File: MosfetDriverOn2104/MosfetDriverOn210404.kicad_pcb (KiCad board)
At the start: 2 copper layers, 83.6 x 89.7 mm, 88 parts, among them J1 I2C HDR, J10 ENCODER HDR, J11 CROSS CONN, J12 motor, J2 AVR-ISP-6, J3 I2C HDR, J4 Screw_Terminal_01x02, J5 I2C HDR, J6 UART HDR, J7 5V HDR, J8 GND HDR, J9 servo hdr, Q1 IRF540N, Q2 IRF540N, Q3 IRF540N, Q4 IRF540N, SW1 SW_Push, SW2 SW_DIP_x04, SW3 SW_Push, SW4 SW_Push, U1 LM2576HVS-ADJ, U2 L7805, U3 IR2104, U4 LM358, U5 IR2104, U6 ATmega328P-AU-MCU_Microchip_A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

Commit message: Tested Route capability
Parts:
- moved CB6 11.5 mm to (141.8, 100.7), turned to 0 degrees
- moved R10 0.51 mm to (149.3, 128.3)
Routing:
- net GND: track 0.00 -> 495.8 mm, vias 0 -> 1
- net VCC: track 0.00 -> 225.2 mm
- net +5V: track 0.00 -> 177.9 mm, vias 0 -> 3
- net +15V: track 0.00 -> 149.8 mm, vias 0 -> 1
- net /IS+: track 0.00 -> 134.7 mm, vias 0 -> 1
- net /M1: track 0.00 -> 78.1 mm
- net /RST: track 0.00 -> 65.8 mm, vias 0 -> 1
- net /M2: track 0.00 -> 47.6 mm
- net Net-(D1-Pad1): track 0.00 -> 38.6 mm
- net /~SD: track 0.00 -> 38.5 mm, vias 0 -> 1
- net /SGN1: track 0.00 -> 34.8 mm
- net Net-(C9-Pad1): track 0.00 -> 30.4 mm
- net /SGN2: track 0.00 -> 27.2 mm
- net Net-(SW2-Pad1): track 0.00 -> 25.2 mm
- net Net-(D5-Pad1): track 0.00 -> 23.8 mm
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
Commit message: placements altered
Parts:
- moved D3 1.26 mm to (156.0, 87.2), turned to 180 degrees
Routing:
- net +15V: track 149.8 -> 145.7 mm
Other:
- net class Default: clearance 0.2 -> 0.3; trace_width 0.25 -> 0.4; via_dia 0.8 -> 1; via_drill 0.4 -> 0.8
- net class power added: clearance 0.3, trace_width 0.81, via_dia 1.2, via_drill 0.8
- rule trace_clearance: 0.2 -> 0.3
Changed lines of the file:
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@@
-(kicad_pcb (version 20171130) (host pcbnew "(5.0.0)")
+(kicad_pcb (version 20171130) (host pcbnew "(5.0.1)-3")
   (general
     (thickness 1.6)
     (drawings 5)
-    (tracks 751)
+    (tracks 750)
     (zones 0)
     (modules 88)
@@
   )
   (setup
-    (last_trace_width 0.25)
-    (trace_clearance 0.2)
+    (last_trace_width 0.4)
+    (trace_clearance 0.3)
     (zone_clearance 0.508)
     (zone_45_only no)
@@
     (segment_width 0.2)
     (edge_width 0.15)
-    (via_size 0.8)
-    (via_drill 0.4)
+    (via_size 1)
+    (via_drill 0.8)
     (via_min_size 0.4)
     (via_min_drill 0.3)
@@
   (net 59 "Net-(J6-Pad3)")
   (net_class Default "This is the default net class."
-    (clearance 0.2)
-    (trace_width 0.25)
-    (via_dia 0.8)
-    (via_drill 0.4)
+    (clearance 0.3)
+    (trace_width 0.4)
+    (via_dia 1)
+    (via_drill 0.8)
     (uvia_dia 0.3)
     (uvia_drill 0.1)
@@
     (add_net VCC)
   )
+  (net_class power ""
+    (clearance 0.3)
+    (trace_width 0.81)
+    (via_dia 1.2)
+    (via_drill 0.8)
+    (uvia_dia 0.3)
+    (uvia_drill 0.1)
+  )
   (module Capacitor_SMD:CP_Elec_5x5.3 (layer F.Cu)
     (at 136.398 94.783 90)
@@
   )
   (module Diode_SMD:D_SMA (layer F.Cu)
-    (at 155.874945 85.995 150)
+    (at 155.988 87.249 180)
     (descr "Diode SMA (DO-214AC)")
     (tags "Diode SMA (DO-214AC)")
     (attr smd)
-    (fp_text reference D3 (at 0 -2.5 150) (layer F.SilkS)
+    (fp_text reference D3 (at 0 -2.5 180) (layer F.SilkS)
       (effects (font (size 1 1) (thickness 0.15)))
     )
-    (fp_text value D (at 0 2.600001 150) (layer F.Fab)
+    (fp_text value D (at 0 2.600001 180) (layer F.Fab)
       (effects (font (size 1 1) (thickness 0.15)))
     )
@@
     (fp_line (start 2.3 1.5) (end -2.3 1.5) (layer F.Fab) (width 0.1))
     (fp_line (start -3.4 -1.65) (end -3.4 1.65) (layer F.SilkS) (width 0.12))
-    (fp_text user %R (at 0 -2.5 150) (layer F.Fab)
+    (fp_text user %R (at 0 -2.5 180) (layer F.Fab)
       (effects (font (size 1 1) (thickness 0.15)))
     )
-    (pad 2 smd rect (at 2.000001 -0.000001 150) (size 2.5 1.8) (layers F.Cu F.Paste F.Mask)
+    (pad 2 smd rect (at 2.000001 -0.000001 180) (size 2.5 1.8) (layers F.Cu F.Paste F.Mask)
       (net 3 +15V))
-    (pad 1 smd rect (at -2.000001 0.000001 150) (size 2.5 1.8) (layers F.Cu F.Paste F.Mask)
+    (pad 1 smd rect (at -2.000001 0.000001 180) (size 2.5 1.8) (layers F.Cu F.Paste F.Mask)
       (net 18 "Net-(C8-Pad1)"))
     (model ${KISYS3DMOD}/Diode_SMD.3dshapes/D_SMA.wrl
@@
     (fp_line (start 3.048 -4.318) (end 7.112 -4.318) (layer F.SilkS) (width 0.15))
     (fp_line (start -2.032 -4.318) (end 2.032 -4.318) (layer F.SilkS) (width 0.15))
-    (fp_line (start -7.112 -4.318) (end -3.048 -4.318) (layer F.SilkS) (width 0.15))
+    (fp_line (start -7.112 -4.318) (end -3.047999 -4.318) (layer F.SilkS) (width 0.15))
     (fp_line (start 2.032 -15.748) (end 2.032 -4.318) (layer F.SilkS) (width 0.15))
-    (fp_line (start 3.048 -15.748) (end 2.032 -15.748) (layer F.SilkS) (width 0.15))
-    (fp_line (start 3.048 -4.318) (end 3.048 -15.748) (layer F.SilkS) (width 0.15))
+    (fp_line (start 3.048 -15.748001) (end 2.032 -15.748) (layer F.SilkS) (width 0.15))
+    (fp_line (start 3.048 -4.318) (end 3.048 -15.748001) (layer F.SilkS) (width 0.15))
     (fp_line (start -2.032 -15.748) (end -2.032 -4.318) (layer F.SilkS) (width 0.15))
-    (fp_line (start -3.048 -15.748) (end -2.032 -15.748) (layer F.SilkS) (width 0.15))
-    (fp_line (start -3.048 -4.318) (end -3.048 -15.748) (layer F.SilkS) (width 0.15))
+    (fp_line (start -3.048 -15.747999) (end -2.032 -15.748) (layer F.SilkS) (width 0.15))
+    (fp_line (start -3.047999 -4.318) (end -3.048 -15.747999) (layer F.SilkS) (width 0.15))
     (fp_line (start 7.112 -15.748) (end 7.112 -4.318) (layer F.SilkS) (width 0.15))
     (fp_line (start 8.128 -15.748) (end 7.112 -15.748) (layer F.SilkS) (width 0.15))
@@
     (fp_line (start -8.128 -15.748) (end -8.128 -3.048) (layer F.SilkS) (width 0.15))
     (fp_line (start 8.128 -3.048) (end -8.128 -3.048) (layer F.SilkS) (width 0.15))
-    (fp_line (start 1.778 -2.286) (end -1.778 -2.286) (layer F.SilkS) (width 0.15))
-    (fp_line (start 0 -2.286) (end 1.778 -2.286) (layer F.SilkS) (width 0.15))
+    (fp_line (start 1.778001 -2.286) (end -1.778 -2.286) (layer F.SilkS) (width 0.15))
+    (fp_line (start 0 -2.286) (end 1.778001 -2.286) (layer F.SilkS) (width 0.15))
     (fp_line (start 5.334 -1.778) (end -5.334 -1.778) (layer F.SilkS) (width 0.15))
     (fp_line (start 5.334 2.032) (end 5.334 0) (layer F.SilkS) (width 0.15))
@@
   (segment (start 151.638 87.219002) (end 151.608002 87.249) (width 0.25) (layer F.Cu) (net 3))
   (segment (start 151.638 85.344) (end 151.638 87.219002) (width 0.25) (layer F.Cu) (net 3))
-  (segment (start 151.987 84.995) (end 151.638 85.344) (width 0.25) (layer F.Cu) (net 3))
-  (segment (start 154.142893 84.995) (end 151.987 84.995) (width 0.25) (layer F.Cu) (net 3))
   (segment (start 152.508 90.805) (end 152.908 90.805) (width 0.25) (layer B.Cu) (net 3))
   (segment (start 150.8252 92.4878) (end 152.508 90.805) (width 0.25) (layer B.Cu) (net 3))
@@
   (segment (start 107.5944 117.2464) (end 108.2548 117.9068) (width 0.25) (layer F.Cu) (net 3))
   (segment (start 112.1664 117.9068) (end 118.7704 124.5108) (width 0.25) (layer F.Cu) (net 3))
-  (segment (start 146.216 86.995) (end 148.336 84.875) (width 0.25) (layer F.Cu) (net 3))
-  (segment (start 144.716 86.995) (end 146.216 86.995) (width 0.25) (layer F.Cu) (net 3))
-  (segment (start 148.336 84.875) (end 148.336 84.0232) (width 0.25) (layer F.Cu) (net 3))
-  (segment (start 148.336 84.0232) (end 149.1996 83.1596) (width 0.25) (layer F.Cu) (net 3))
-  (segment (start 152.307493 83.1596) (end 154.142893 84.995) (width 0.25) (layer F.Cu) (net 3))
-  (segment (start 149.1996 83.1596) (end 152.307493 83.1596) (width 0.25) (layer F.Cu) (net 3))
   (segment (start 114.046 112.5728) (end 126.3904 100.2284) (width 0.25) (layer B.Cu) (net 3))
   (segment (start 147.14 98.044) (end 148.59 98.044) (width 0.25) (layer B.Cu) (net 3))
   (segment (start 144.9556 100.2284) (end 147.14 98.044) (width 0.25) (layer B.Cu) (net 3))
   (segment (start 126.3904 100.2284) (end 144.9556 100.2284) (width 0.25) (layer B.Cu) (net 3))
+  (segment (start 152.082998 85.344) (end 151.638 85.344) (width 0.25) (layer F.Cu) (net 3))
+  (segment (start 146.216 86.995) (end 148.336 84.875) (width 0.25) (layer F.Cu) (net 3))
+  (segment (start 144.716 86.995) (end 146.216 86.995) (width 0.25) (layer F.Cu) (net 3))
+  (segment (start 148.336 84.875) (end 148.336 84.0232) (width 0.25) (layer F.Cu) (net 3))
+  (segment (start 148.336 84.0232) (end 149.1996 83.1596) (width 0.25) (layer F.Cu) (net 3))
+  (segment (start 149.1996 83.1596) (end 149.898598 83.1596) (width 0.25) (layer F.Cu) (net 3))
+  (segment (start 149.898598 83.1596) (end 152.082998 85.344) (width 0.25) (layer F.Cu) (net 3))
   (segment (start 152.273 105.575003) (end 152.273 107.696) (width 0.25) (layer F.Cu) (net 4))
   (segment (start 152.273001 104.775002) (end 152.273 105.575003) (width 0.25) (layer F.Cu) (net 4))

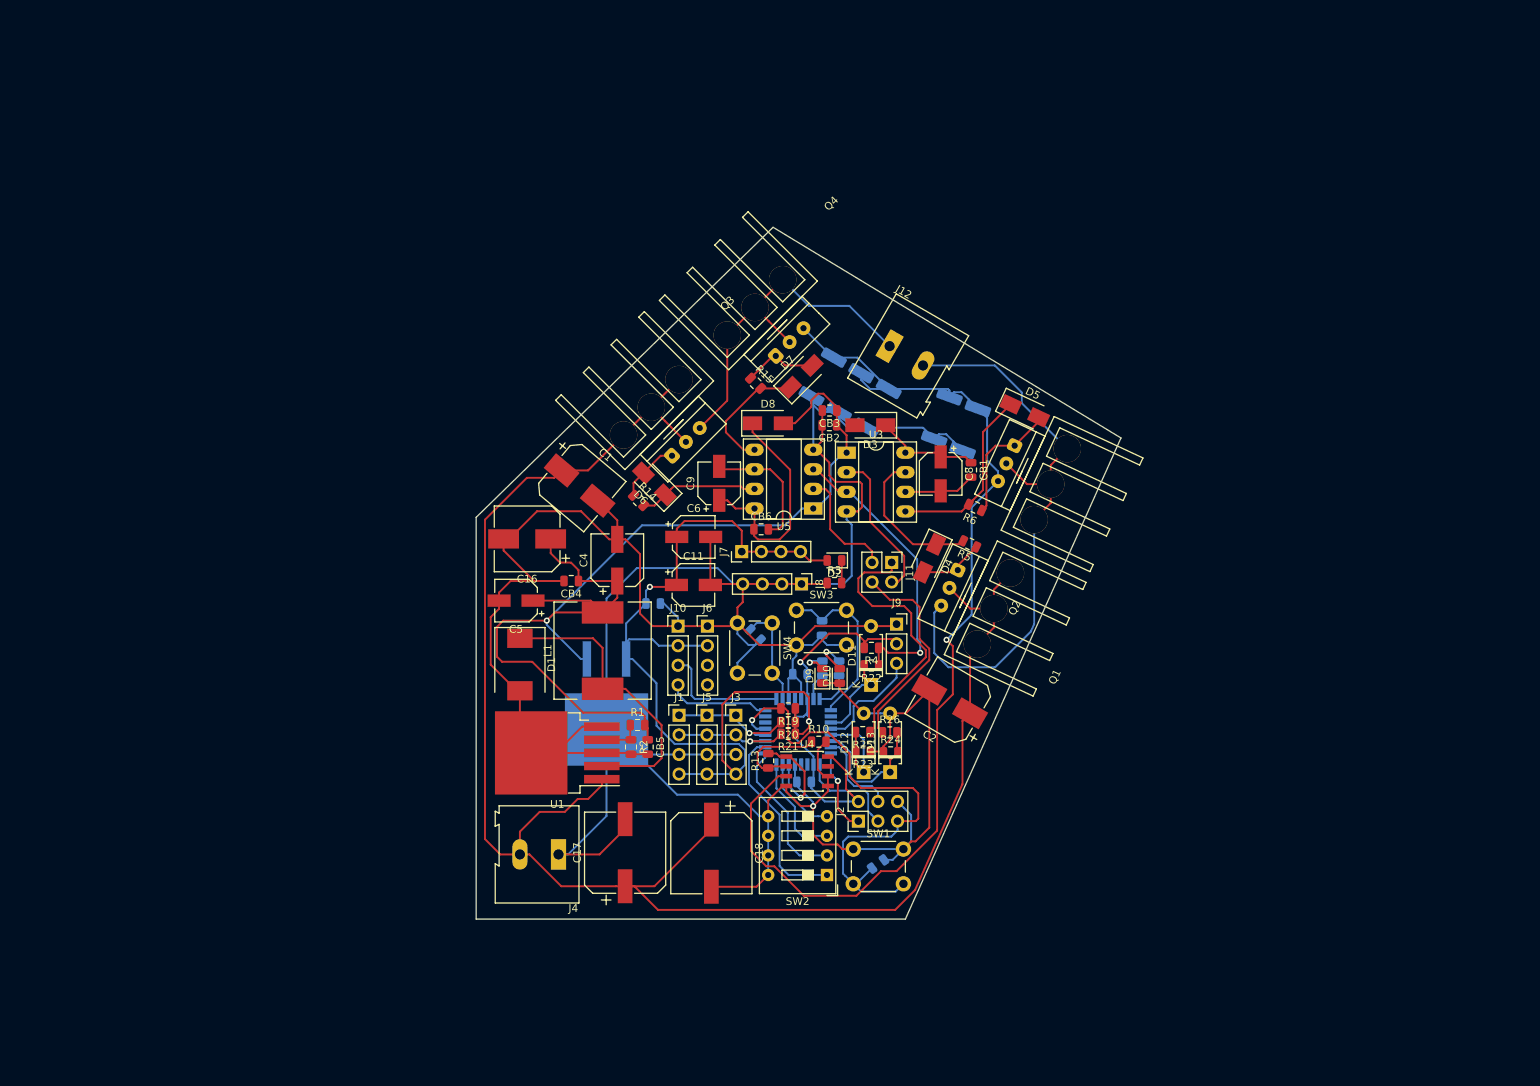
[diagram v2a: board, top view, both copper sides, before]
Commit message: Applying different packing strategy
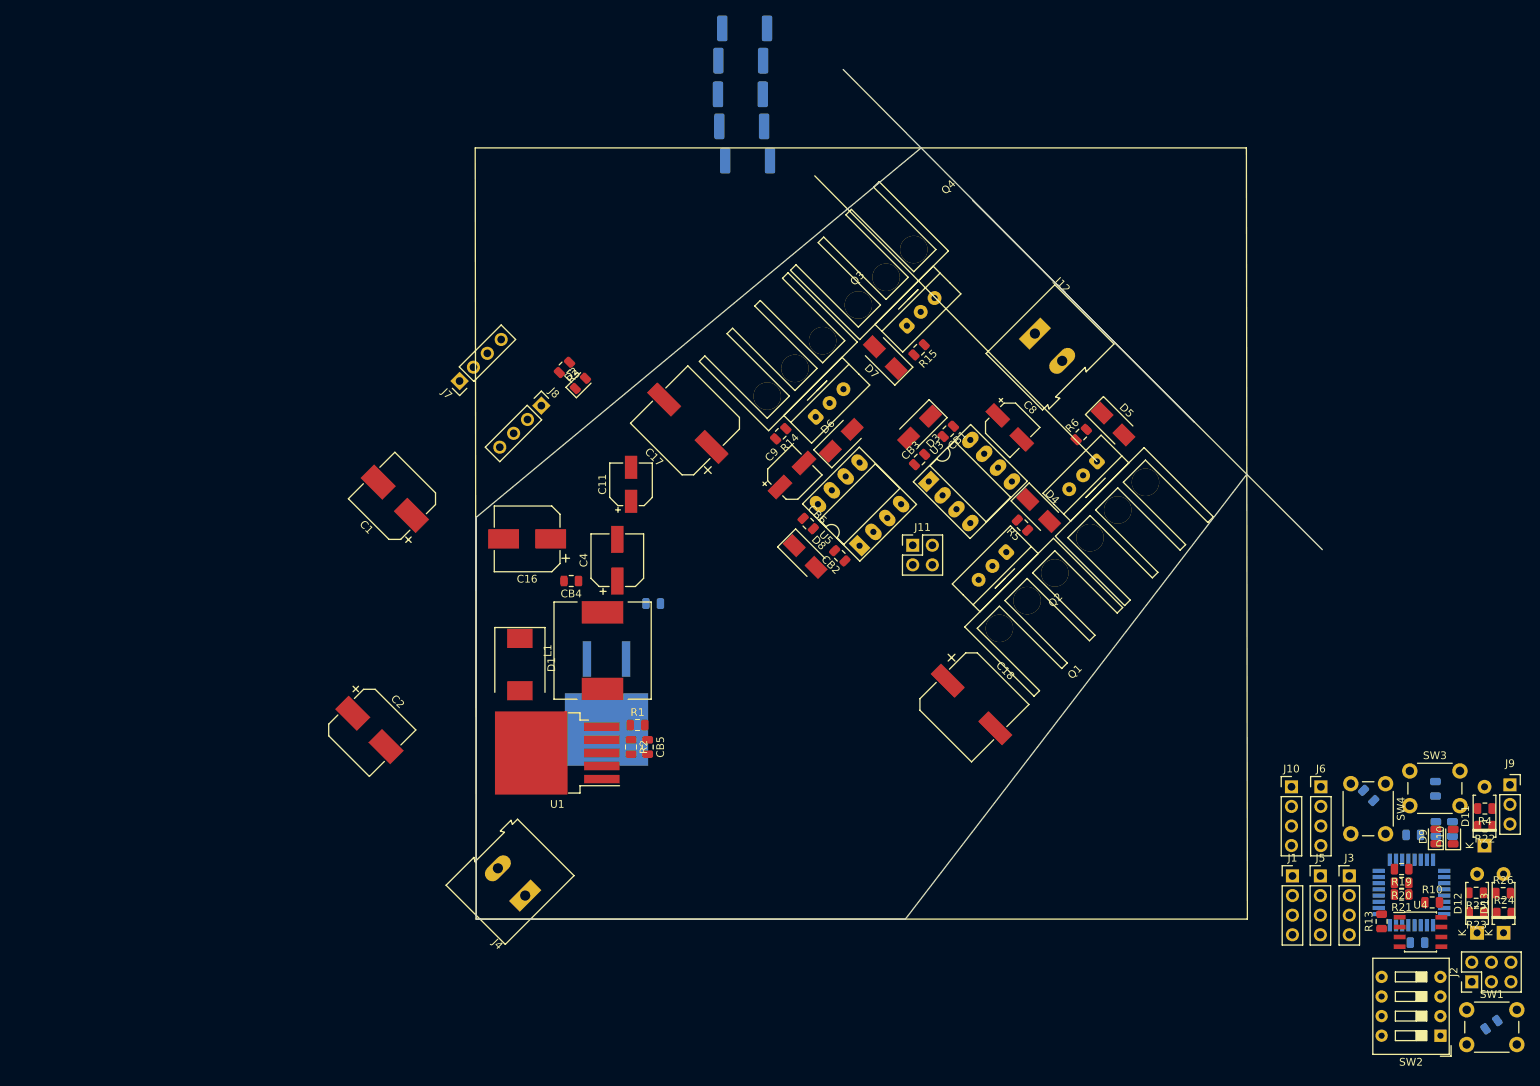
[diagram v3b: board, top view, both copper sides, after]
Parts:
- removed C5, C6: CP, Capacitor_SMD:CP_Elec_5x5.4
- Q1, Q2, Q3, Q4: footprint Footprints:TO220_HS_SCREW -> TO220_HS_SCREW:TO220_HS_SCREW
- moved C14 82.2 mm to (229.2, 134.4)
- moved C15 82.2 mm to (220.6, 135.2)
- moved C7 82.2 mm to (226.4, 140.3)
- moved D11 82.2 mm to (235.6, 141.7)
- moved D12 82.2 mm to (234.6, 153.0)
- moved D13 82.2 mm to (238.1, 153.0)
- moved J1 82.2 mm to (210.7, 145.7)
- moved J2 82.2 mm to (233.9, 159.4)
- moved J3 82.2 mm to (218.1, 145.7)
- moved J5 82.2 mm to (214.3, 145.7)
- moved J9 82.2 mm to (238.9, 133.9)
- moved R10 82.2 mm to (228.8, 149.1)
- moved R13 82.2 mm to (222.3, 151.6)
- moved R17 82.2 mm to (229.3, 139.6)
- moved R18 82.2 mm to (231.4, 139.6)
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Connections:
- J6 pad 3: Net-(J6-Pad3) -> (no net)
- J6 pad 4: Net-(J6-Pad4) -> (no net)
- U4 pad 7: Net-(U4-Pad7) -> (no net)
- U6 pad 10: Net-(U6-Pad10) -> (no net)
- U6 pad 19: Net-(U6-Pad19) -> (no net)
- U6 pad 20: Net-(U6-Pad20) -> (no net)
- U6 pad 30: /RX -> (no net)
- U6 pad 31: /TX -> (no net)
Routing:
- net GND: track 495.8 -> 0.00 mm, vias 1 -> 0
- net VCC: track 225.2 -> 0.00 mm
- net +5V: track 177.9 -> 0.00 mm, vias 3 -> 0
- net +15V: track 145.7 -> 0.00 mm, vias 1 -> 0
- net /IS+: track 134.7 -> 0.00 mm, vias 1 -> 0
- net /M1: track 78.1 -> 0.00 mm
- net /RST: track 65.8 -> 0.00 mm, vias 1 -> 0
- net /M2: track 47.6 -> 0.00 mm
- net Net-(D1-Pad1): track 38.6 -> 0.00 mm
- net /~SD: track 38.5 -> 0.00 mm, vias 1 -> 0
- net /SGN1: track 34.8 -> 0.00 mm
- net Net-(C9-Pad1): track 30.4 -> 0.00 mm
- net /SGN2: track 27.2 -> 0.00 mm
- net Net-(SW2-Pad1): track 25.2 -> 0.00 mm
- net Net-(D5-Pad1): track 23.8 -> 0.00 mm
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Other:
- board size 83.6 x 89.7 mm -> 109.7 x 110.1 mm

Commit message: Almost moved everything in
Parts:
- C10, C12, C13, C14, C15, C7, R17, R18, U6: moved to F.Cu
- C16: footprint Capacitor_SMD:CP_Elec_8x6.2 -> Capacitor_SMD:CP_Elec_10x7.9
- moved SW1 119.8 mm to (127.1, 107.4), turned to 315 degrees
- moved C10 115.7 mm to (131.8, 115.5), turned to 45 degrees
- moved SW2 103.1 mm to (141.0, 114.2), turned to 45 degrees
- moved J6 100.1 mm to (115.4, 119.4), turned to 135 degrees
- moved SW4 100.0 mm to (123.0, 127.7), turned to 45 degrees
- moved D9 98.5 mm to (131.2, 131.3), turned to 315 degrees
- moved D10 97.9 mm to (133.9, 134.0), turned to 315 degrees
- moved J3 97.0 mm to (130.2, 104.5), turned to 135 degrees
- moved D13 96.4 mm to (144.9, 128.1), turned to 315 degrees
- moved R19 95.6 mm to (132.9, 118.6), turned to 315 degrees
- moved R20 95.1 mm to (134.4, 117.1), turned to 315 degrees
- moved R21 94.9 mm to (135.5, 116.1), turned to 315 degrees
- moved R18 94.8 mm to (136.9, 132.6), turned to 225 degrees
- moved C14 94.2 mm to (135.3, 141.7), turned to 135 degrees
- moved R17 94.2 mm to (135.5, 131.1), turned to 225 degrees
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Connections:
- J6 pad 3: (no net) -> /TX
- J6 pad 4: (no net) -> /RX
- U6 pad 30: (no net) -> /RX
- U6 pad 31: (no net) -> /TX
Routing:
- net /M1: track 0.00 -> 79.6 mm
- net VCC: track 0.00 -> 52.5 mm
- net /M2: track 0.00 -> 51.1 mm
- net GND: track 0.00 -> 45.2 mm
- net /IS+: track 0.00 -> 32.0 mm
- net +15V: track 0.00 -> 24.1 mm
- net Net-(D5-Pad1): track 0.00 -> 21.1 mm
- net Net-(C8-Pad2): track 0.00 -> 20.6 mm
- net Net-(D6-Pad1): track 0.00 -> 19.7 mm
- net Net-(D7-Pad1): track 0.00 -> 17.8 mm
- net Net-(C9-Pad2): track 0.00 -> 17.1 mm
- net Net-(D4-Pad1): track 0.00 -> 14.8 mm
- net Net-(C9-Pad1): track 0.00 -> 11.9 mm
- net Net-(C8-Pad1): track 0.00 -> 11.4 mm
- net Net-(D6-Pad2): track 0.00 -> 9.91 mm
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- added copper zone on B.Cu, net GND
- added copper zone on F.Cu, net GND
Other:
- board size 109.7 x 110.1 mm -> 99.9 x 99.9 mm

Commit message: Routing done...
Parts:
- added J13: Conn_01x02_Female, Connector_PinHeader_2.54mm:PinHeader_1x02_P2.54mm_Vertical, F.Cu at (141.0, 98.2)
- U2: footprint Package_TO_SOT_SMD:TO-263-2 -> Package_TO_SOT_SMD:SOT-223-3_TabPin2; moved to F.Cu
- moved C11 105.7 mm to (163.9, 113.9), turned to 45 degrees
- moved U2 87.1 mm to (157.1, 109.4), turned to 315 degrees
- moved J7 86.4 mm to (137.2, 145.8), turned to 225 degrees
- moved C2 82.4 mm to (173.4, 125.8), turned to 225 degrees
- moved C16 79.3 mm to (113.2, 121.9)
- moved C4 68.7 mm to (137.2, 93.6), turned to 45 degrees
- moved R3 65.3 mm to (133.2, 136.7)
- moved J4 65.1 mm to (111.7, 148.3)
- moved D2 64.5 mm to (134.6, 138.2)
- moved L1 61.6 mm to (129.1, 102.1), turned to 45 degrees
- moved D1 60.5 mm to (120.8, 95.5), turned to 225 degrees
- moved R1 53.8 mm to (125.0, 111.1), turned to 315 degrees
- moved R2 51.5 mm to (122.4, 112.5), turned to 225 degrees
- moved C18 50.5 mm to (121.5, 140.2)
- moved U1 50.4 mm to (115.1, 106.3), turned to 135 degrees
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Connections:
- J11 pad 1: /SGN1 -> /SGN2
- J11 pad 4: /SGN2 -> /SGN1
- R23 pad 2: Net-(D12-Pad1) -> /SGN1
- R24 pad 2: Net-(D13-Pad1) -> /SGN2
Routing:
- net +5V: track 0.00 -> 218.7 mm
- net VCC: track 52.5 -> 256.9 mm, vias 0 -> 2
- net +15V: track 24.1 -> 146.2 mm, vias 0 -> 1
- net GND: track 45.2 -> 121.9 mm, vias 0 -> 162
- net /~SD: track 0.00 -> 70.9 mm, vias 0 -> 2
- net /IS+: track 32.0 -> 90.5 mm, vias 0 -> 1
- net /SGN2: track 0.00 -> 47.6 mm
- net /SGN1: track 0.00 -> 46.9 mm
- net /RST: track 0.00 -> 45.5 mm, vias 0 -> 1
- net Net-(D1-Pad1): track 0.00 -> 34.3 mm
- net Net-(C14-Pad1): track 0.00 -> 26.0 mm
- net /SCL: track 0.00 -> 23.1 mm
- net /Isense: track 0.00 -> 22.2 mm
- net /SDA: track 0.00 -> 20.9 mm
- net Net-(C15-Pad1): track 0.00 -> 18.2 mm
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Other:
- net class Default: clearance 0.3 -> 0.2; trace_width 0.4 -> 0.25
- net class power removed
- rule trace_clearance: 0.3 -> 0.2

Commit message: Completed Route
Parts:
- added REF**: MountingHole_3.2mm_M3, MountingHole:MountingHole_3.2mm_M3, F.Cu at (128.9, 147.8)
- added REF**: MountingHole_3.2mm_M3, MountingHole:MountingHole_3.2mm_M3, F.Cu at (108.6, 112.8)
- added REF**: MountingHole_3.2mm_M3, MountingHole:MountingHole_3.2mm_M3, F.Cu at (162.3, 56.9)
- added REF**: MountingHole_3.2mm_M3, MountingHole:MountingHole_3.2mm_M3, F.Cu at (199.4, 93.9)
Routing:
- net GND: vias 162 -> 153
